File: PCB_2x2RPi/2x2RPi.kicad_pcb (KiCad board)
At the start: 2 copper layers, 44.5 x 50.8 mm, 21 parts, among them P1 VIN, P2 CONN_13X2, P3 VIN, P4 REL1, P5 REL2, P6 INPUT, P7 5V, SW1 PWR SW, U1 LowCurVReg, U2 LowCurVReg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

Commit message: Added Power Switch to BOM
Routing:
- net NoConnection1: track 0.00 -> 22.3 mm
- net (no net): track 22.3 -> 0.00 mm
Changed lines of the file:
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@@
     (links 51)
     (no_connects 0)
-    (area 94.752524 45.677001 146.425921 101.803201)
+    (area 89.164524 45.677001 146.425921 106.14)
     (thickness 1.6)
-    (drawings 16)
+    (drawings 18)
     (tracks 299)
     (zones 0)
@@
     (visible_elements 7FFFFFFF)
     (pcbplotparams
-      (layerselection 283672577)
-      (usegerberextensions true)
-      (excludeedgelayer true)
+      (layerselection 295698432)
+      (usegerberextensions false)
+      (excludeedgelayer false)
       (linewidth 152400)
       (plotframeref false)
       (viasonmask false)
       (mode 1)
-      (useauxorigin true)
+      (useauxorigin false)
       (hpglpennumber 1)
       (hpglpenspeed 20)
@@
       (psnegative false)
       (psa4output false)
-      (plotreference true)
-      (plotvalue true)
-      (plotothertext true)
+      (plotreference false)
+      (plotvalue false)
+      (plotothertext false)
       (plotinvisibletext false)
       (padsonsilk false)
       (subtractmaskfromsilk false)
-      (outputformat 1)
+      (outputformat 2)
       (mirror false)
-      (drillshape 0)
+      (drillshape 2)
       (scaleselection 1)
-      (outputdirectory gerbers/))
-  )
-  (net 0 "")
+      (outputdirectory drawings/))
+  )
+  (net 0 NoConnection1)
   (net 1 /12V)
   (net 2 /3V3)
@@
     (uvia_dia 0.508)
     (uvia_drill 0.127)
-    (add_net "")
     (add_net /3V3)
     (add_net /5V-Relay1)
@@
     (add_net N-000003)
     (add_net N-000004)
+    (add_net NoConnection1)
   )
   (net_class PWR ""
@@
     )
   )
+  (dimension 7.112 (width 0.25) (layer Dwgs.User)
+    (gr_text "0.2800 in" (at 106.680002 46.752001) (layer Dwgs.User)
+      (effects (font (size 1 1) (thickness 0.25)))
+    )
+    (feature1 (pts (xy 110.236 100.076) (xy 110.236002 45.752001)))
+    (feature2 (pts (xy 103.124 100.076) (xy 103.124002 45.752001)))
+    (crossbar (pts (xy 103.124002 47.752001) (xy 110.236002 47.752001)))
+    (arrow1a (pts (xy 110.236002 47.752001) (xy 109.109499 48.338421)))
+    (arrow1b (pts (xy 110.236002 47.752001) (xy 109.109499 47.165581)))
+    (arrow2a (pts (xy 103.124002 47.752001) (xy 104.250505 48.338421)))
+    (arrow2b (pts (xy 103.124002 47.752001) (xy 104.250505 47.165581)))
+  )
+  (dimension 44.45 (width 0.25) (layer Dwgs.User)
+    (gr_text "1.7500 in" (at 123.825 105.139999) (layer Dwgs.User)
+      (effects (font (size 1 1) (thickness 0.25)))
+    )
+    (feature1 (pts (xy 146.05 101.6) (xy 146.05 106.139999)))
+    (feature2 (pts (xy 101.6 101.6) (xy 101.6 106.139999)))
+    (crossbar (pts (xy 101.6 104.139999) (xy 146.05 104.139999)))
+    (arrow1a (pts (xy 146.05 104.139999) (xy 144.923497 104.726419)))
+    (arrow1b (pts (xy 146.05 104.139999) (xy 144.923497 103.553579)))
+    (arrow2a (pts (xy 101.6 104.139999) (xy 102.726503 104.726419)))
+    (arrow2b (pts (xy 101.6 104.139999) (xy 102.726503 103.553579)))
+  )
+  (dimension 50.8 (width 0.25) (layer Dwgs.User)
+    (gr_text "2.0000 in" (at 92.98 76.2 90) (layer Dwgs.User)
+      (effects (font (size 1 1) (thickness 0.25)))
+    )
+    (feature1 (pts (xy 101.6 50.8) (xy 91.98 50.8)))
+    (feature2 (pts (xy 101.6 101.6) (xy 91.98 101.6)))
+    (crossbar (pts (xy 93.98 101.6) (xy 93.98 50.8)))
+    (arrow1a (pts (xy 93.98 50.8) (xy 94.56642 51.926503)))
+    (arrow1b (pts (xy 93.98 50.8) (xy 93.39358 51.926503)))
+    (arrow2a (pts (xy 93.98 101.6) (xy 94.56642 100.473497)))
+    (arrow2b (pts (xy 93.98 101.6) (xy 93.39358 100.473497)))
+  )
   (gr_text "2x2RPi\nIHE    ilt3.com" (at 139.319 75.3745) (layer F.SilkS)
     (effects (font (size 1 1) (thickness 0.25)))
@@
     (arrow2b (pts (xy 99.568 100.076) (xy 98.98158 98.949497)))
   )
-  (dimension 7.112 (width 0.25) (layer Dwgs.User)
-    (gr_text "0.2800 in" (at 106.680002 46.752001) (layer Dwgs.User)
-      (effects (font (size 1 1) (thickness 0.25)))
-    )
-    (feature1 (pts (xy 110.236 100.076) (xy 110.236002 45.752001)))
-    (feature2 (pts (xy 103.124 100.076) (xy 103.124002 45.752001)))
-    (crossbar (pts (xy 103.124002 47.752001) (xy 110.236002 47.752001)))
-    (arrow1a (pts (xy 110.236002 47.752001) (xy 109.109499 48.338421)))
-    (arrow1b (pts (xy 110.236002 47.752001) (xy 109.109499 47.165581)))
-    (arrow2a (pts (xy 103.124002 47.752001) (xy 104.250505 48.338421)))
-    (arrow2b (pts (xy 103.124002 47.752001) (xy 104.250505 47.165581)))
-  )
   (gr_line (start 101.6 50.8) (end 101.6 101.6) (angle 90) (layer Edge.Cuts) (width 0.15))

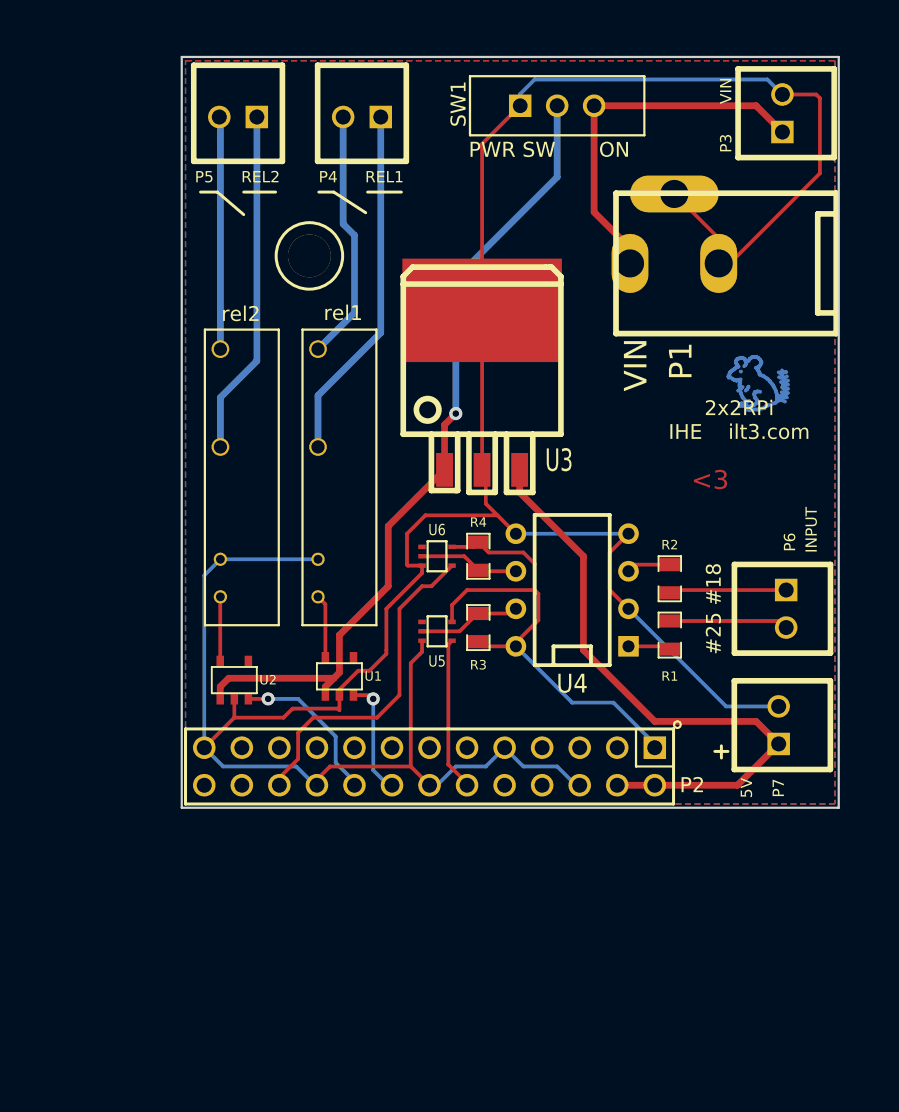
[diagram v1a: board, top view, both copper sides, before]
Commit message: Adding relay limiting resistor
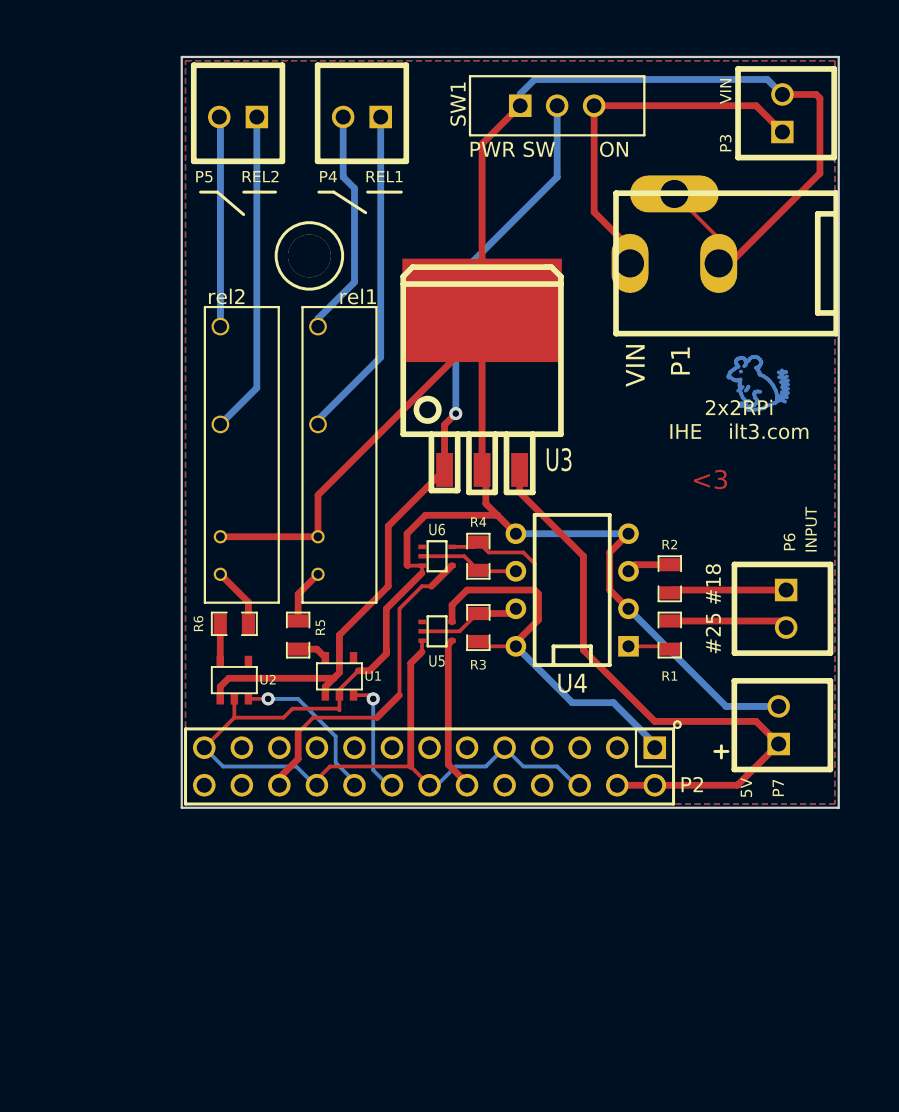
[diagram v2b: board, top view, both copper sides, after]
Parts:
- added R5: R, SM0805_NonPol, F.Cu at (109.5, 89.9)
- added R6: R, SM0805_NonPol, F.Cu at (105.2, 89.2)
- moved rel1 1.52 mm to (112.3, 77.7)
- moved rel2 1.52 mm to (105.7, 77.7)
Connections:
- P1 pad 3: GND -> (no net)
- P2 pad 10: (no net) -> N-0000034
- P2 pad 11: (no net) -> N-0000029
- P2 pad 13: (no net) -> N-0000028
- P2 pad 15: (no net) -> N-0000027
- P2 pad 17: (no net) -> N-0000026
- P2 pad 19: (no net) -> N-0000025
- P2 pad 21: (no net) -> N-0000024
- P2 pad 23: (no net) -> N-0000023
- P2 pad 24: (no net) -> N-0000021
- P2 pad 26: (no net) -> N-0000022
- P2 pad 3: (no net) -> N-0000031
- P2 pad 5: (no net) -> N-0000032
- P2 pad 7: (no net) -> N-0000030
- P2 pad 8: (no net) -> N-0000033
- U5 pad 1: (no net) -> N-0000011
- U6 pad 1: (no net) -> N-0000014
- rel1 pad 1: /5V-Relay1 -> N-0000016
- rel2 pad 1: /5V-Relay2 -> N-0000017
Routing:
- net NoConnection1: track 22.3 -> 0.00 mm
- net (no net): track 0.00 -> 22.3 mm
- net GND: track 192.4 -> 199.1 mm
- net N-0000017: track 0.00 -> 4.13 mm
- net N-0000016: track 0.00 -> 3.72 mm
- net /5V-Relay1: track 4.32 -> 2.08 mm
- net /5V-Relay2: track 4.37 -> 2.54 mm
- net N-000009: track 15.7 -> 14.2 mm
- net N-000008: track 23.3 -> 21.8 mm
- net N-0000037: track 17.0 -> 15.5 mm
- net N-0000036: track 24.1 -> 22.6 mm
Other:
- net class Default: trace_width 0.254 -> 0.4572

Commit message: Updating 2x2RPi not finished yet
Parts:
- added D1: DIODE, LED SMD 0805, F.Cu at (131.2, 113.4)
- added D2: DIODE, LED SMD 0805, F.Cu at (125.9, 118.1)
- added D3: DIODE, LED SMD 0805, F.Cu at (131.4, 117.6)
- added F1: FUSE, SM0805_NonPol, F.Cu at (116.6, 109.4)
- added J1: USB, USB micro-female, F.Cu at (143.8, 111.5)
- added P8: CONN_13, pin_array_13x1, F.Cu at (119.6, 104.8)
- added P9: GND, PIN_ARRAY_2X1_Screw Terminal, F.Cu at (107.8, 114.5)
- added R7: R, SM0805_NonPol, F.Cu at (125.2, 111.9)
- added R8: R, SM0805_NonPol, F.Cu at (123.8, 114.4)
- added R9: R, SM0805_NonPol, F.Cu at (133.1, 110.6)
- P3: value VIN -> CONN_13; footprint PIN_ARRAY_2X1_Screw Terminal -> pin_array_13x1
- moved P3 47.1 mm to (119.5, 95.9), turned to 180 degrees
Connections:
- P1 pad 1: /V_IN -> /5Vreg
- P2 pad 11: N-0000029 -> N-0000032
- P2 pad 13: N-0000028 -> N-0000031
- P2 pad 15: N-0000027 -> N-0000030
- P2 pad 17: N-0000026 -> N-0000028
- P2 pad 19: N-0000025 -> N-0000029
- P2 pad 21: N-0000024 -> N-0000026
- P2 pad 23: N-0000023 (its old number) -> N-0000024
- P2 pad 3: N-0000031 -> N-0000035
- P2 pad 5: N-0000032 -> N-0000034
- P2 pad 7: N-0000030 -> N-0000033
- P3 pad 1: /V_IN -> /3V3
- P3 pad 2: GND -> N-0000035
- R5 pad 1: /5V-Relay1 -> N-000002
- R6 pad 1: /5V-Relay2 -> N-000007
- SW1 pad 2: /12V -> N-0000013
- SW1 pad 3: /V_IN -> /5Vreg
- U1 pad 1: /12V -> /5V-RPI
- U2 pad 1: /12V -> /5V-RPI
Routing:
- net GND: track 199.1 -> 0.00 mm
- net /12V: track 55.1 -> 0.00 mm, vias 1 -> 0
- net /5V-RPI: track 41.9 -> 0.00 mm
- net /3V3: track 34.9 -> 0.00 mm
- net /V_IN: track 25.2 -> 0.00 mm
- net /GPIO_25: track 22.6 -> 0.00 mm
- net N-0000042: track 22.6 -> 0.00 mm
- net (no net): track 22.3 -> 0.00 mm
- net N-0000044: track 21.8 -> 0.00 mm
- net N-0000041: track 15.5 -> 0.00 mm
- net N-0000043: track 14.2 -> 0.00 mm
- net /GPIO_24: track 10.8 -> 0.00 mm, vias 1 -> 0
- net /GPIO_18: track 10.4 -> 0.00 mm
- net /IN_18: track 8.06 -> 0.00 mm
- net /GPIO_23: track 7.96 -> 0.00 mm, vias 1 -> 0
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
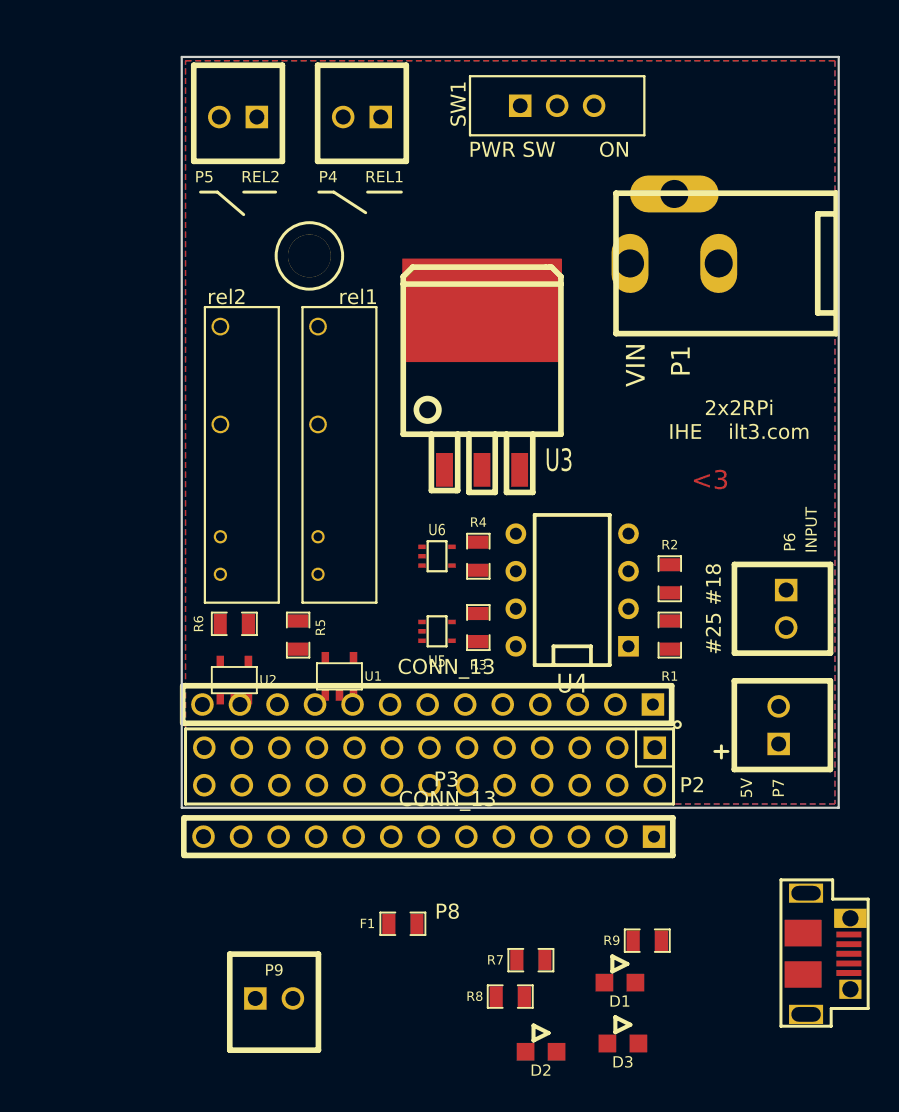
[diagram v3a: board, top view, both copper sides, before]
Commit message: Adding new revisino 2x2RPi board
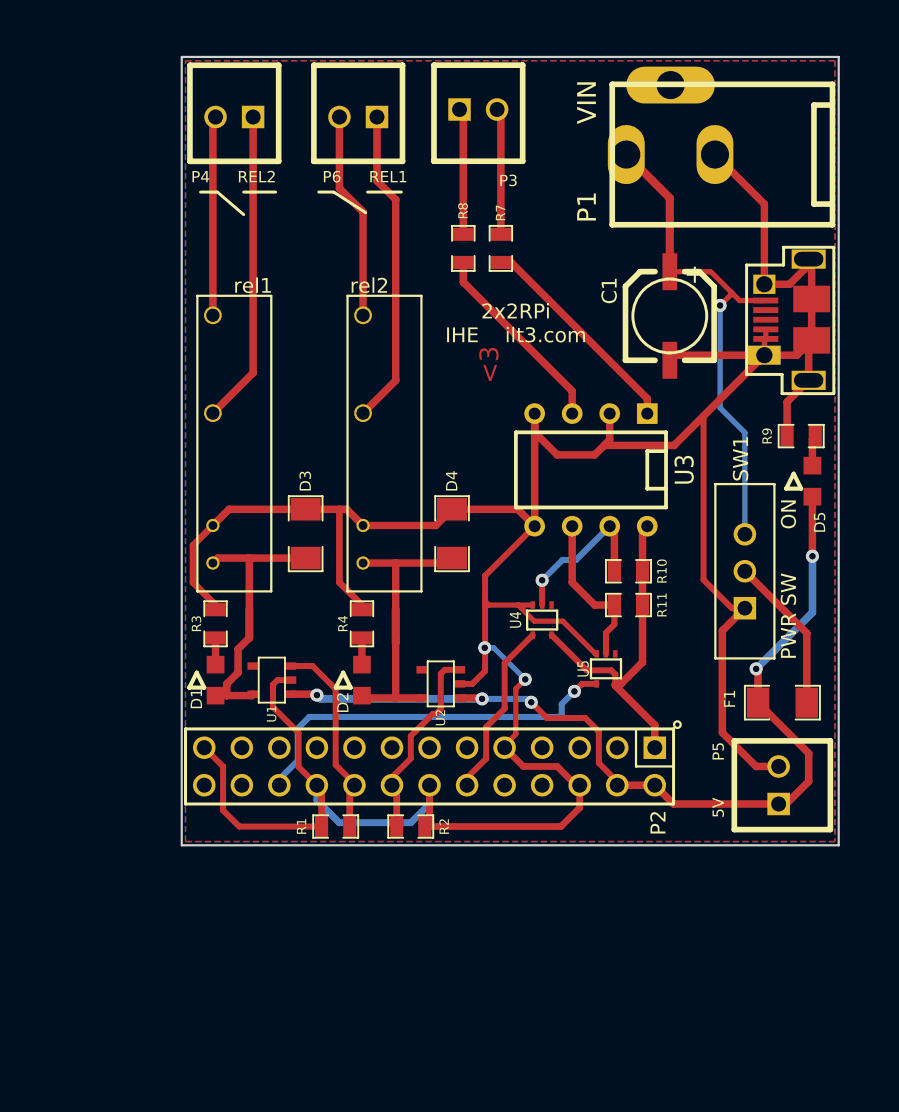
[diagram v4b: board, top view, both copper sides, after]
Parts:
- removed 1PIN: P***, 1pin_NPTH_Mechanical
- removed P7: 5V, PIN_ARRAY_2X1_Screw Terminal
- removed P8: CONN_13, pin_array_13x1
- removed P9: GND, PIN_ARRAY_2X1_Screw Terminal
- removed R5, R6: R, SM0805_NonPol
- removed U6: INVERTER-1CH, SOT353
- added C1: 10uF, SMD_CAP_5m, F.Cu at (134.6, 68.3)
- added D4: DIODE, SM1206, F.Cu at (119.9, 83.1)
- added D5: LED, LED SMD 0805, F.Cu at (144.3, 79.5)
- added R10: 1k, SM0805_NonPol, F.Cu at (131.8, 85.6)
- added R11: 1k, SM0805_NonPol, F.Cu at (131.8, 87.9)
- D1, D2: value DIODE -> LED
- D3: footprint LED SMD 0805 -> SM1206
- F1: footprint SM0805_NonPol -> SM1206
- P3: value CONN_13 -> INPUT; footprint pin_array_13x1 -> PIN_ARRAY_2X1_Screw Terminal
- P4: value REL1 -> REL2
- P5: value REL2 -> 5V
- P6: value INPUT -> REL1
- R1, R2: value 680 -> 1k
- R3, R4: value R -> 330
- R7, R8: value R -> 680
- R9: value R -> 1k
- U3: value 7805-TO263 -> TLP2531; footprint TO263 -> DIP-8__300
- U4: value TLP2531 -> INVERTER-1CH; footprint DIP-8__300 -> SOT353
- moved P5 58.2 mm to (142.0, 100.1), turned to 90 degrees
- moved R8 50.7 mm to (120.7, 63.8), turned to 270 degrees
- moved R7 48.2 mm to (123.2, 63.8), turned to 270 degrees
- moved P6 44.1 mm to (113.5, 54.9), turned to 180 degrees
- moved J1 42.9 mm to (144.0, 68.6), turned to 180 degrees
- moved P3 41.6 mm to (121.7, 54.4), turned to 0 degrees
- moved D3 40.6 mm to (110.0, 83.1), turned to 270 degrees
- moved R9 35.7 mm to (143.5, 76.5)
- moved D1 34.2 mm to (103.9, 93.0), turned to 90 degrees
- moved SW1 34.0 mm to (139.7, 85.6), turned to 90 degrees
- moved F1 29.7 mm to (142.2, 94.5), turned to 180 degrees
- moved D2 27.9 mm to (113.8, 93.0), turned to 90 degrees
- moved R1 26.1 mm to (112.0, 102.9), turned to 0 degrees
- moved R2 24.3 mm to (117.1, 102.9), turned to 180 degrees
- moved R3 17.8 mm to (103.9, 89.2)
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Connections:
- D1 pad 1: /5V-Relay1 -> /5V-Relay2
- D1 pad 2: N-000002 -> N-0000011
- D2 pad 1: /5V-Relay2 -> /5V-Relay1
- D2 pad 2: N-000007 (its old number) -> N-0000023
- D3 pad 1: /5V-RPI -> GND
- D3 pad 2: N-000005 -> /5V-Relay2
- P2 pad 11: N-0000032 -> N-0000016
- P2 pad 13: N-0000031 -> N-0000010
- P2 pad 15: N-0000030 -> N-000002
- P2 pad 17: N-0000028 -> N-000003
- P2 pad 19: N-0000029 -> N-000004
- P2 pad 21: N-0000026 (its old number) -> N-000005
- P2 pad 23: N-0000024 -> N-000006
- P2 pad 3: N-0000035 -> N-0000013
- P2 pad 5: N-0000034 -> N-0000014
- P2 pad 7: N-0000033 -> N-0000015
- P3 pad 1: /3V3 -> /IN_25
- P3 pad 2: N-0000035 -> /IN_18
- P5 pad 1: N-0000044 -> /5V-RPI
- P5 pad 2: N-0000043 -> GND
- P6 pad 1: /IN_25 -> N-0000029
- P6 pad 2: /IN_18 -> N-0000028
- R1 pad 1: /IN_18 -> GND
- R1 pad 2: N-0000011 -> /GPIO_24
- R2 pad 1: /IN_25 -> GND
- R2 pad 2: N-0000010 -> /GPIO_23
- R3 pad 1: N-0000039 -> GND
- R3 pad 2: /3V3 -> N-0000011
- R4 pad 1: N-0000040 -> GND
- R4 pad 2: /3V3 -> N-0000023
- R7 pad 1: GND -> /IN_18
- R7 pad 2: /GPIO_23 -> N-0000034
- R8 pad 1: GND -> /IN_25
- R8 pad 2: /GPIO_24 -> N-0000033
- R9 pad 2: N-000005 -> N-0000021
- U1 pad 3: /GPIO_23 -> /GPIO_24
- U1 pad 5: /5V-Relay1 -> /5V-Relay2
- U2 pad 3: /GPIO_24 -> /GPIO_23
- U2 pad 5: /5V-Relay2 -> /5V-Relay1
- U3 pad 1: /12V -> N-0000034
- U3 pad 3: /5V-RPI -> N-0000033
- U4 pad 1: N-0000011 -> N-0000040
- U4 pad 2: GND -> N-0000032
- U4 pad 3: N-0000010 -> GND
- U4 pad 4: GND -> /GPIO_18
- U4 pad 5: GND -> /3V3
- U5 pad 2: N-0000039 -> N-0000031
- U5 pad 4: /GPIO_18 -> /GPIO_25
- rel1 pad 1: N-0000012 -> /5V-Relay2
- rel2 pad 1: N-000004 -> /5V-Relay1
- rel2 pad 3: N-0000044 -> N-0000029
- rel2 pad 4: N-0000043 -> N-0000028
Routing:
- net GND: track 0.00 -> 226.8 mm, vias 0 -> 2
- net /5V-RPI: track 0.00 -> 64.0 mm, vias 0 -> 5
- net /5Vreg: track 0.00 -> 33.8 mm, vias 0 -> 1
- net /GPIO_25: track 0.00 -> 26.3 mm, vias 0 -> 1
- net /3V3: track 0.00 -> 23.3 mm
- net N-0000029: track 0.00 -> 21.5 mm
- net N-0000026: track 0.00 -> 21.2 mm
- net /5V-Relay1: track 0.00 -> 19.8 mm
- net /5V-Relay2: track 0.00 -> 19.2 mm
- net N-0000034: track 0.00 -> 14.7 mm
- net N-0000028: track 0.00 -> 14.1 mm
- net /GPIO_24: track 0.00 -> 13.6 mm
- net N-0000027: track 0.00 -> 13.5 mm
- net /GPIO_23: track 0.00 -> 13.3 mm
- net N-0000033: track 0.00 -> 13.3 mm
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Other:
- board size 44.5 x 50.8 mm -> 44.5 x 53.3 mm
- net class Default: trace_width 0.4572 -> 0.5588
- net class PWR removed

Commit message: 2nd revision 2x2RPi board and gerber files, awaiting approval
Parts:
- removed P5: 5V, PIN_ARRAY_2X1_Screw Terminal
- added 1PIN: P***, 1pin_NPTH_Mechanical_M3_Screw, F.Cu at (110.2, 64.3)
- moved D2 10.8 mm to (103.1, 91.4)
- moved D3 10.8 mm to (99.3, 81.5)
- moved D4 10.8 mm to (109.2, 81.5)
- moved F1 10.8 mm to (131.6, 93.0)
- moved J1 10.8 mm to (133.3, 67.1)
- moved R4 10.8 mm to (103.1, 87.6)
- moved U2 10.8 mm to (108.5, 91.7)
- moved U3 10.8 mm to (118.6, 77.2)
- moved rel1 10.8 mm to (94.5, 75.4)
- moved rel2 10.8 mm to (104.6, 75.4)
- moved C1 10.8 mm to (124.0, 66.8)
- moved D1 10.8 mm to (93.2, 91.4)
- moved P3 10.8 mm to (111.0, 52.8)
- moved R10 10.8 mm to (121.2, 84.1)
- moved R11 10.8 mm to (121.2, 86.4)
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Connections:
- P1 pad 3: (no net) -> GND
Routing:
- net /GPIO_24: track 13.6 -> 28.2 mm
- net /3V3: track 23.3 -> 34.0 mm
- net /GPIO_25: track 26.3 -> 15.8 mm
- net N-0000034: track 14.7 -> 8.31 mm
- net /IN_25: track 8.55 -> 14.7 mm
- net N-0000033: track 13.3 -> 7.15 mm
- net /IN_18: track 8.55 -> 14.6 mm
- net /GPIO_23: track 13.3 -> 17.9 mm
- net GND: track 226.8 -> 222.4 mm, vias 2 -> 1
- net /5V-RPI: track 64.0 -> 67.4 mm, vias 5 -> 4
- net /5Vreg: track 33.8 -> 37.2 mm
- net /GPIO_18: track 12.0 -> 15.3 mm, vias 0 -> 1
- net N-0000032: track 10.9 -> 9.61 mm, vias 1 -> 0
- net /5V-Relay2: track 19.2 -> 18.4 mm
- net N-0000031: track 10.8 -> 11.5 mm, vias 0 -> 1
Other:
- board size 44.5 x 53.3 mm -> 44.4 x 53.3 mm
